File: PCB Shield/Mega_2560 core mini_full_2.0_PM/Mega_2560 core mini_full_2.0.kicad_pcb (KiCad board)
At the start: 2 copper layers, 89.5 x 59.7 mm, 110 parts, among them P1 2560-core, P10 SPI_libre, P11 Trim, P12 Stick_left, P13 Stick_right, P14 Switch, P15 LCD_I2C, P16 LCD, P17 Battery LIPO, P18 Ecolage, P19 Module_TX, P2 Clock, P20 Module_RS232/TTL, P21 Sw_power, P22 CONN_JQ6500_28P_mini, P23 Rot_1, P24 Rot_2, P25 Key_select_menu_ESC, P26 LCD_Vcc_select, P27 HP, P28 5v/3,3v manches, P3 Option, P4 Potentiometre, P5 Vibreur, P6 Micro_sd, P7 Option, P8 Audio, P9 SPI, U1 4066, U2 TLP290, U3 TLP290, U4 L4941, U5 LD1117S33TR, U6 MCP604-I/SL

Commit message: Update _Mega_2560 core mini_full_2.0_PM
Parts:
- removed the P8 at (205.6, 64.4)
- added C12: 100nF, Capacitors_SMD:C_1206, B.Cu at (150.6, 111.5)
- added C13: 100nF, Capacitors_SMD:C_1206, B.Cu at (149.8, 101.1)
- added C14: 100nF, Capacitors_SMD:C_1206, F.Cu at (149.8, 101.1)
- added P24: Rot_2, Pin_Headers:Pin_Header_Straight_1x04_Pitch2.54mm, F.Cu at (226.5, 112.7)
- added P29: RXTX, Pin_Headers:Pin_Header_Straight_1x04_Pitch2.54mm, F.Cu at (210.7, 98.7)
- added P30: MiniDCDC3A, MegaCore_Shield:MiniDCDC3A, F.Cu at (208.8, 64.4)
- C10, C11, C5, C9, P21: moved to B.Cu
- P12, P13: footprint Pin_Headers:Pin_Header_Straight_1x04_Pitch2.54mm -> MegaCore_Shield:Pin_Header_Straight_2x03_Pitch2.54mm
- P17: value Battery LIPO -> BATT
- P20: value Module_RS232/TTL -> TTL/RS232; footprint anthoperso:Con_RS232_TTL -> MegaCore_Shield:Con_RS232_TTL
- P25: value Key_select_menu_ESC -> Keys
- P26: value LCD_Vcc_select -> LCD_Alim
- P4: value Potentiometre -> 3 Pots; footprint Pin_Headers:Pin_Header_Straight_2x05_Pitch2.54mm -> MegaCore_Shield:Pin_Header_Straight_3x03_Pitch2.54mm
- P7: value Option -> HF_modules; footprint Pin_Headers:Pin_Header_Straight_1x06_Pitch2.54mm -> MegaCore_Shield:Pin_Header_Straight_1x09_Pitch2.54mm
- P8: renamed from P24; value Rot_2 -> Audio
- R7: moved to F.Cu
- U2: footprint anthoperso:SOP4 -> MegaCore_Shield:SOP4
- moved P8 52.6 mm to (205.6, 64.4), turned to 0 degrees
- moved R9 19.1 mm to (194.8, 111.4)
- moved P17 15.9 mm to (205.6, 78.4), turned to 180 degrees
- moved C2 15.5 mm to (218.5, 103.8)
- moved P26 14.6 mm to (226.5, 101.9), turned to 270 degrees
- moved RV6 14.4 mm to (159.9, 66.3), turned to 180 degrees
- moved P3 12.8 mm to (216.4, 110.1)
- moved D2 11.7 mm to (218.3, 91.1)
- moved P19 5.68 mm to (218.3, 88.5)
- moved R7 5.43 mm to (218.3, 93.6)
- moved RV1 4.62 mm to (149.7, 115.2), turned to 180 degrees
- moved C9 4.58 mm to (144.0, 70.8)
- moved C11 4.37 mm to (144.0, 80.7)
- moved C17 3.70 mm to (148.4, 80.3), turned to 270 degrees
- moved P25 3.59 mm to (205.6, 88.5), turned to 90 degrees
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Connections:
- net Net-(C28-Pad1) renamed /DCDC_IN+
- net Net-(P17-Pad2) renamed /LIPO+
- C11 pad 1: /Power_manches -> /Stick_LHcon
- C11 pad 2: /Stick_LVcon -> GND
- C16 pad 1: /Power_manches -> /Stick_RHcon
- C16 pad 2: /Stick_RHcon -> GND
- C17 pad 1: /Power_manches -> /Stick_RVcon
- C17 pad 2: /Stick_RVcon -> GND
- C9 pad 1: /Power_manches -> /Stick_LVcon
- C9 pad 2: /Stick_LHcon -> GND
- D6 pad 2: +BATT -> /R16_R17
- P1 pad D4: (no net) -> /CS_CYRF6936
- P12 pad 2: /Stick_LHcon -> /Power_manches
- P12 pad 4: GND -> /Stick_LHcon
- P13 pad 2: /Stick_RHcon -> /Power_manches
- P13 pad 3: /Stick_RVcon -> /Stick_RHcon
- P13 pad 4: GND -> /Stick_RVcon
- P20 pad 1: GND -> /RX_module
- P20 pad 2: VCC -> /TX_module
- P20 pad 3: Net-(P20-Pad3) -> VCC
- P20 pad 4: Net-(P20-Pad4) -> GND
- P20 pad 5: GND -> Net-(P20-Pad5)
- P20 pad 6: VCC -> Net-(P20-Pad6)
- P20 pad 7: /TX_module -> VCC
- P20 pad 8: /RX_module -> GND
- P21 pad 1: +BATT -> /R16_R17
- P4 pad 2: /Pot_2 -> /Pot_3
- P4 pad 3: VCC -> GND
- P4 pad 4: /Pot_3 -> VCC
- P4 pad 5: VCC -> /Pot_2
- P4 pad 6: /Pot_1 -> GND
- P4 pad 7: GND -> VCC
- P4 pad 8: GND -> /Pot_1
- P7 pad 1: /Microsd_CS -> /P3_3V
- P7 pad 2: /Sck -> GND
- P7 pad 3: /Mosi -> /Sck
- P7 pad 4: /Miso -> /Mosi
- P7 pad 5: VCC -> /Miso
- P7 pad 6: GND -> /CS_CYRF6936
- P8 pad 1: /Rot_2push -> Net-(P8-Pad1)
- P8 pad 2: /Rot_2B -> Net-(P8-Pad2)
- P8 pad 3: /Rot_2A -> VCC
- R17 pad 2: +BATT -> /R16_R17
- U2 pad 3: Net-(P20-Pad3) -> Net-(P20-Pad6)
- U3 pad 4: Net-(P20-Pad4) -> Net-(P20-Pad5)
- U5 pad 4: (no net) -> /P3_3V
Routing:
- net +BATT: track 35.7 -> 6.53 mm
- net /P3_3V: track 105.3 -> 129.4 mm, vias 4 -> 2
- net GND: track 77.9 -> 101.3 mm, vias 20 -> 16
- net /Vibreur: track 2.36 -> 22.3 mm
- net Net-(D1-Pad1): track 32.4 -> 13.4 mm
- net /Lcd_bla: track 42.7 -> 26.2 mm, vias 2 -> 0
- net Net-(P16-Pad18): track 34.7 -> 48.9 mm, vias 3 -> 4
- net /PPM_out: track 39.3 -> 53.3 mm
- net /R16_R17: track 0.00 -> 11.7 mm
- net /Key_ESC: track 6.77 -> 18.4 mm, vias 0 -> 1
- net VCC: track 376.4 -> 387.4 mm, vias 12 -> 14
- net /Key_MENU: track 6.77 -> 17.7 mm, vias 0 -> 1
- net /Lcd_A0: track 69.7 -> 59.4 mm
- net /DCDC_IN+: track 12.1 -> 22.3 mm
- net Net-(P20-Pad6): track 0.00 -> 9.97 mm
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- added copper zone on B.Cu, net /P3_3V
- added copper zone on F.Cu, net /P3_3V
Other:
- board text added: "5 3,3"
- board text added: "By OpenAVRc Team"
- board text added: "ICSP"
- board text added: "MegaCore2560 Shield V2.0"
- board text removed: "3.3v"
- board text removed: "MegaCore2560 Shield"
- board text removed: "OpenAVRc Team V2.0"

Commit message: Update_Mega_2560 core mini_full_2.0_PM_23-8-2017
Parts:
- added BT1: CR2032, Pin_Headers:Pin_Header_Straight_1x02_Pitch2.54mm, F.Cu at (197.3, 106.3)
- added C15: 100nF, Capacitors_SMD:C_1206, F.Cu at (197.5, 116.1)
- added C18: 100nF, Capacitors_SMD:C_1206, F.Cu at (175.0, 82.1)
- added C19: 100nF, Capacitors_SMD:C_1206, B.Cu at (167.1, 117.3)
- added C20: 100nF, Capacitors_SMD:C_1206, B.Cu at (178.5, 117.5)
- added C21: 100nF, Capacitors_SMD:C_1206, B.Cu at (193.3, 117.5)
- added C22: 100nF, Capacitors_SMD:C_1206, B.Cu at (184.6, 99.3)
- added C23: 100nF, Capacitors_SMD:C_1206, B.Cu at (181.5, 106.3)
- added D3: LL4148, MegaCore_Shield:D_SCD80_HandSoldering, F.Cu at (192.9, 94.9)
- added D4: LL4148, MegaCore_Shield:D_SCD80_HandSoldering, F.Cu at (192.9, 96.4)
- added P31: Pot2, Pin_Headers:Pin_Header_Straight_1x03_Pitch2.54mm, F.Cu at (154.1, 106.3)
- added P32: Pot1, Pin_Headers:Pin_Header_Straight_1x03_Pitch2.54mm, F.Cu at (154.1, 103.8)
- added R10: 22K, Resistors_SMD:R_1206, B.Cu at (200.5, 67.0)
- added R15: 10K, anthoperso:R_1206, B.Cu at (186.5, 107.0)
- added R20: 10K, anthoperso:R_1206, B.Cu at (186.5, 103.2)
- added REF**: SOIC-Micro8, MegaCore_Shield:SOIC-Micro8, F.Cu at (243.0, 69.5)
- added REF**: SOT-457, MegaCore_Shield:SOT-457, F.Cu at (243.0, 77.1)
- added U7: FM24W256, MegaCore_Shield:SOIC-8-FRAM_DI, F.Cu at (185.9, 100.0)
- added U8: DS3231, MegaCore_Shield:SO-16-DS3231, F.Cu at (185.9, 108.2)
- added U9: 4050, MegaCore_Shield:SO-16-N, F.Cu at (243.0, 87.9)
- P4: value 3 Pots -> Pot3; footprint MegaCore_Shield:Pin_Header_Straight_3x03_Pitch2.54mm -> Pin_Headers:Pin_Header_Straight_1x03_Pitch2.54mm
- P7: value HF_modules -> SPIX; footprint MegaCore_Shield:Pin_Header_Straight_1x09_Pitch2.54mm -> MegaCore_Shield:Pin_Header_Straight_2x05_Pitch2.54mm
- R2: value 22K -> 1K
- U1: value 4066 -> 74LVC1G3157; footprint Librairie master:SOP14 -> MegaCore_Shield:SOT-363_SC-70-6_Handsoldering
- moved R5 60.0 mm to (238.5, 99.1)
- moved R6 59.8 mm to (244.3, 99.1), turned to 90 degrees
- moved C6 32.7 mm to (192.2, 77.8)
- moved R16 15.9 mm to (208.8, 78.4), turned to 270 degrees
- moved R3 15.4 mm to (176.4, 101.2), turned to 180 degrees
- moved R17 15.3 mm to (211.3, 78.4), turned to 90 degrees
- moved U1 9.09 mm to (184.0, 116.5), turned to 0 degrees
- moved R4 4.49 mm to (178.9, 92.4)
- moved P27 4.07 mm to (197.3, 78.4), turned to 180 degrees
- moved R9 2.90 mm to (197.3, 110.0), turned to 90 degrees
- moved C12 2.85 mm to (149.1, 113.9)
- moved P7 2.84 mm to (179.5, 76.5)
- moved RV1 2.54 mm to (149.7, 117.8)
- moved C38 1.91 mm to (215.1, 75.2)
- moved R8 1.71 mm to (193.5, 110.0), turned to 270 degrees
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- renumbered REF** to Fix1, REF** to Fix2, REF** to Fix3
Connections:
- C38 pad 1: /P3_3V -> P3_3V
- C8 pad 1: /P3_3V -> P3_3V
- D2 pad 2: /PPM_out -> /Master_PPMout
- D6 pad 2: /R16_R17 -> +BATT
- P1 pad A0: /Trim_RH-> -> /Lcd_db0
- P1 pad A1: /Trim_RH<- -> /Lcd_db1
- P1 pad A2: /Trim_RV-> -> /Lcd_db2
- P1 pad A3: /Trim_RV<- -> /Lcd_db3
- P1 pad A4: /Trim_LV-> -> /Lcd_db4
- P1 pad A5: /Trim_LV<- -> /Lcd_db5
- P1 pad A6: /Trim_LH-> -> /Lcd_db6
- P1 pad A7: /Trim_LH<- -> /Lcd_db7
- P1 pad D4: /CS_CYRF6936 -> /PPM_in
- P10 pad 1: /PH2 -> (no net)
- P10 pad 2: /TXD2 -> (no net)
- P10 pad 3: /RXD2 -> (no net)
- P15 pad 3: /Sda -> /SDA
- P15 pad 4: /Scl -> /SCL
- P2 pad 1: /Scl -> /SCL
- P2 pad 2: /Sda -> /SDA
- P21 pad 1: /R16_R17 -> +BATT
- P26 pad 1: /P3_3V -> P3_3V
- P28 pad 3: /P3_3V -> P3_3V
- P3 pad 1: /Scl -> /SCL
- P3 pad 2: /Sda -> /SDA
- P7 pad 1: /P3_3V -> /CS_CC2500
- P7 pad 2: GND -> /CS_CYRF6936
- P7 pad 3: /Sck -> /CS_A7105
- P7 pad 4: /Mosi -> /CS_NRF24L01
- P7 pad 5: /Miso -> /Xmitter_MISO
- P7 pad 6: /CS_CYRF6936 -> /Xmitter_SCK
- P7 pad 7: (no net) -> P3_3V
- P7 pad 8: (no net) -> /Xmitter_MOSI
- P7 pad 9: (no net) -> GND
- R17 pad 2: /R16_R17 -> +BATT
- R3 pad 1: /core_pw10 -> /JQ6500Busy
- R4 pad 1: /core_pw13 -> /JQ6500Data
- R5 pad 1: VCC -> (no net)
- R5 pad 2: Net-(R5-Pad2) -> (no net)
- R6 pad 1: GND -> (no net)
- R6 pad 2: Net-(R6-Pad2) -> (no net)
- U1 pad 1: GND -> /PPM_in
- U1 pad 2: Net-(R5-Pad2) -> GND
- U1 pad 3: Net-(R6-Pad2) -> /Master_PPMout
- U1 pad 4: VCC -> Net-(R8-Pad2)
- U1 pad 5: /Sim_control -> VCC
- U1 pad 6: Net-(R5-Pad2) -> /Sim_Control
- U5 pad 2: /P3_3V -> P3_3V
- U5 pad 4: /P3_3V -> P3_3V
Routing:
- net P3_3V: track 0.00 -> 133.1 mm, vias 0 -> 3
- net /P3_3V: track 129.4 -> 0.00 mm, vias 2 -> 0
- net /Master_PPMout: track 0.00 -> 69.4 mm, vias 0 -> 4
- net GND: track 101.3 -> 160.0 mm, vias 16 -> 21
- net /PPM_out: track 53.3 -> 0.00 mm, vias 2 -> 0
- net /Sim_Control: track 0.00 -> 47.9 mm, vias 0 -> 4
- net /SDA: track 0.00 -> 43.6 mm, vias 0 -> 3
- net /SCL: track 0.00 -> 41.0 mm, vias 0 -> 2
- net /Xmitter_MISO: track 0.00 -> 40.7 mm, vias 0 -> 2
- net /Sim_control: track 36.8 -> 0.00 mm, vias 4 -> 0
- net /JQ6500Data: track 0.00 -> 34.3 mm, vias 0 -> 1
- net /Xmitter_MOSI: track 0.00 -> 34.0 mm, vias 0 -> 2
- net /Xmitter_SCK: track 0.00 -> 29.9 mm, vias 0 -> 3
- net /CS_A7105: track 0.00 -> 29.8 mm, vias 0 -> 2
- net /CS_NRF24L01: track 0.00 -> 29.3 mm, vias 0 -> 2
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- added copper zone on B.Cu, net P3_3V
- added copper zone on F.Cu, net P3_3V
- removed copper zone on B.Cu, net /P3_3V
- removed copper zone on F.Cu, net /P3_3V
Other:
- board text added: "+"
- board text added: "-"

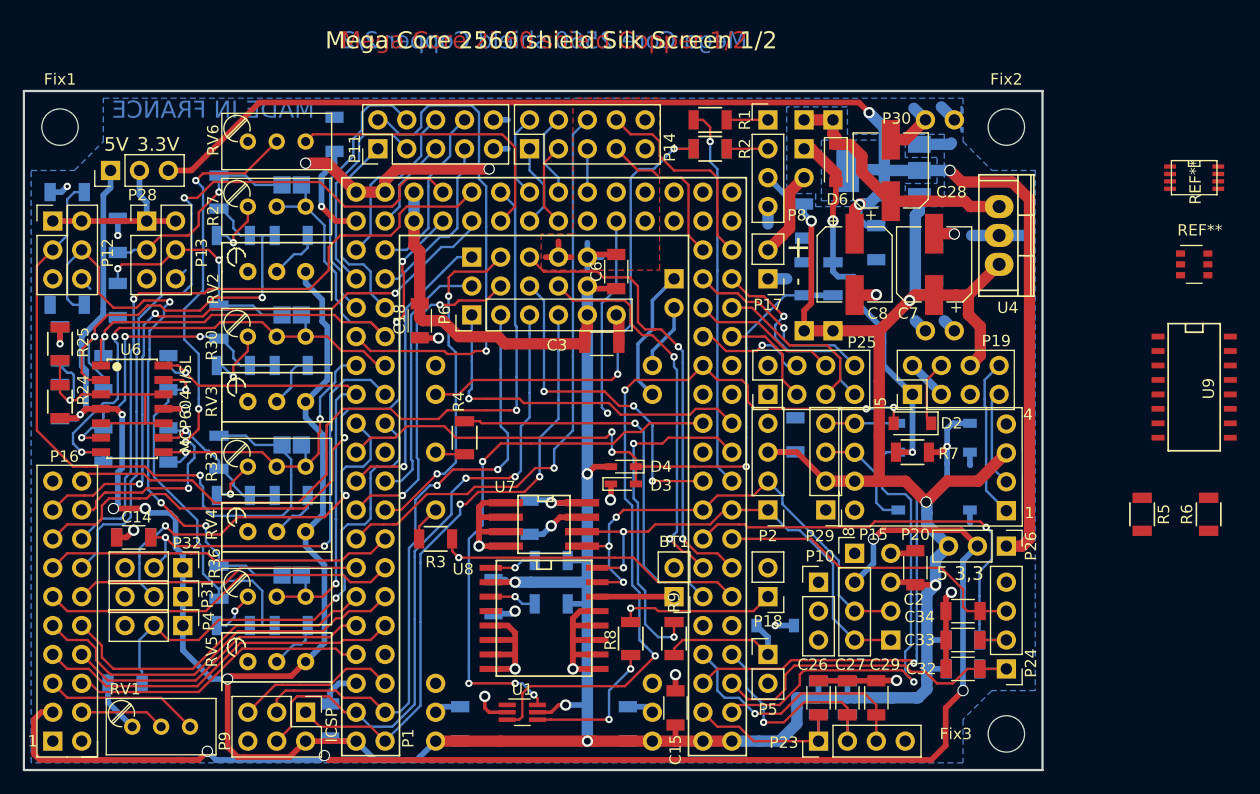
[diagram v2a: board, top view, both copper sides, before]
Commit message: Update schematic R values
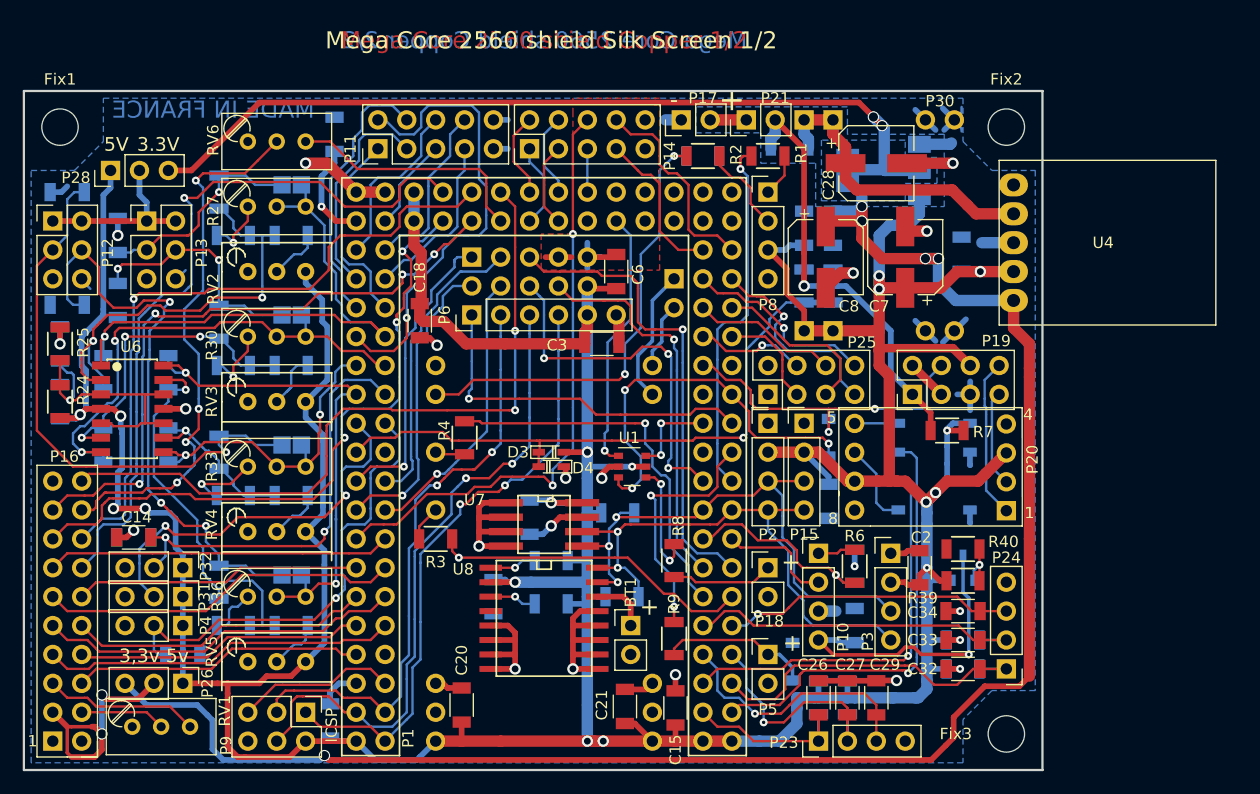
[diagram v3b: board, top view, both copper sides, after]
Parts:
- removed the P10 at (210.0, 105.1)
- removed REF**: SOIC-Micro8, MegaCore_Shield:SOIC-Micro8
- removed the U1 at (184.0, 116.5)
- removed U9: 4050, MegaCore_Shield:SO-16-N
- added C24: 100nF, Capacitors_SMD:C_1206, B.Cu at (213.2, 108.9)
- added Q1: BSS84, MegaCore_Shield:SOT-23_MOS_P, B.Cu at (222.7, 103.8)
- added R21: 4,7K, anthoperso:R_1206, B.Cu at (192.4, 99.0)
- added R38: 4,7K, anthoperso:R_1206, B.Cu at (192.8, 106.3)
- added R39: 47K, Resistors_SMD:R_1206, F.Cu at (222.7, 104.9)
- added R40: 100, Resistors_SMD:R_1206, F.Cu at (222.7, 102.1)
- C1, C2, C3, C5: value 47nF -> 100nF
- C20, C21, P21, P3: moved to F.Cu
- C28, C7: value 47µF -> 100µF
- D2, D6: moved to B.Cu
- P10: renamed from P29; value RXTX -> RX1TX1
- P22: value CONN_JQ6500_28P_mini -> JQ6500_28P
- R11, R12, R13, R14: value 15K -> 120K
- R18, R19, R22, R23: value 5.1k -> 5.1K
- R24: value 33K -> 82K
- R25: value 33K -> 39K
- R26, R29, R32, R35: value 10K -> 47K
- R27, R30, R33, R36: value POT_22k -> 100K
- R28, R31, R34, R37: value 10K -> 120K
- R5: value 10K -> 4K7; moved to B.Cu
- R6: value 10K -> 4K7
- RV2, RV3, RV4, RV5: value POT_100k -> 100K
- U1: renamed from REF**; value SOT-457 -> 74LVC1G3157GV
- U4: value L4941 -> PM5033; footprint Power_Integrations:TO-220 -> MegaCore_Shield:Pm5033_sil5
- U8: value DS3231 -> DS3231SN
- moved P26 73.4 mm to (154.1, 113.9)
- moved U1 52.5 mm to (193.6, 94.9)
- moved R6 31.4 mm to (213.2, 103.7)
- moved R5 25.7 mm to (213.2, 103.7)
- moved P17 15.9 mm to (198.0, 64.4), turned to 90 degrees
- moved P15 12.3 mm to (208.8, 91.1)
- moved R8 7.85 mm to (197.3, 103.2), turned to 90 degrees
- moved P2 7.62 mm to (205.6, 91.1), turned to 0 degrees
- moved P3 7.62 mm to (216.4, 102.5)
- moved D2 7.47 mm to (210.9, 92.4), turned to 270 degrees
- moved C1 6.53 mm to (210.9, 97.9), turned to 90 degrees
- moved D4 6.53 mm to (186.5, 94.9), turned to 180 degrees
- moved D3 6.48 mm to (186.5, 93.6), turned to 0 degrees
- moved P8 6.35 mm to (205.6, 70.8)
- moved R1 5.99 mm to (205.6, 67.6)
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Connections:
- net /CS_CC2500 renamed CS_CC2500
- net /Isp_rst renamed /OpenAVRc_CoreConnects/Isp_rst
- net /JQ6500Busy renamed JQ6500Busy
- net /JQ6500Data renamed JQ6500Data
- net /Key_DOWN renamed Key_DOWN
- net /Key_ESC renamed Key_ESC
- net /Key_LEFT renamed Key_LEFT
- net /Key_MENU renamed Key_MENU
- net /Key_RIGHT renamed Key_RIGHT
- net /Key_UP renamed Key_UP
- net /Lcd_A0 renamed /OpenAVRc_CoreConnects/Lcd_A0
- net /Lcd_bla renamed /OpenAVRc_CoreConnects/Lcd_bla
- net /Lcd_cs renamed /OpenAVRc_CoreConnects/Lcd_cs
- net /Lcd_db0 renamed /OpenAVRc_CoreConnects/Lcd_db0
- net /Lcd_db1 renamed /OpenAVRc_CoreConnects/Lcd_db1
- net /Lcd_db2 renamed /OpenAVRc_CoreConnects/Lcd_db2
- net /Lcd_db3 renamed /OpenAVRc_CoreConnects/Lcd_db3
- net /Lcd_db4 renamed /OpenAVRc_CoreConnects/Lcd_db4
- net /Lcd_db5 renamed /OpenAVRc_CoreConnects/Lcd_db5
- net /Lcd_db6 renamed /OpenAVRc_CoreConnects/Lcd_db6
- net /Lcd_db7 renamed /OpenAVRc_CoreConnects/Lcd_db7
- net /Lcd_e renamed /OpenAVRc_CoreConnects/Lcd_e
- net /Lcd_r/w renamed /OpenAVRc_CoreConnects/Lcd_r/w
- net /Lcd_rst renamed /OpenAVRc_CoreConnects/Lcd_rst
- net /Lcd_vo renamed /OpenAVRc_CoreConnects/Lcd_vo
- net /Microsd_CS renamed /OpenAVRc_CoreConnects/Microsd_CS
- net /Miso renamed /OpenAVRc_CoreConnects/Miso
- net /Mosi renamed /OpenAVRc_CoreConnects/Mosi
- net /Pot_1 renamed Pot_1
- net /Pot_2 renamed Pot_2
- net /Pot_3 renamed Pot_3
- net /Power_manches renamed /OpenAVRc_Sticks/Power_manches
- net /RX_module renamed /OpenAVRc_HF_Telemetry/RX_module
- net /Rot_1A renamed Rot_1A
- net /Rot_1B renamed Rot_1B
- net /Rot_1push renamed Rot_1push
- net /Rot_2push renamed Rot_2push
- net /Sck renamed /OpenAVRc_CoreConnects/Sck
- net /Stick_LH renamed Stick_LH
- net /Stick_LHcon renamed /OpenAVRc_Sticks/Stick_LHcon
- net /Stick_LV renamed Stick_LV
- net /Stick_LVcon renamed /OpenAVRc_Sticks/Stick_LVcon
- net /Stick_RH renamed Stick_RH
- net /Stick_RHcon renamed /OpenAVRc_Sticks/Stick_RHcon
- net /Stick_RV renamed Stick_RV
- net /Stick_RVcon renamed /OpenAVRc_Sticks/Stick_RVcon
- net /Sw_ailDR renamed Sw_ailDR
- net /Sw_eleDR renamed Sw_eleDR
- net /Sw_gear renamed Sw_gear
- net /Sw_id1 renamed Sw_id1
- net /Sw_id2 renamed Sw_id2
- net /Sw_rudDR renamed Sw_rudDR
- net /Sw_thcut renamed Sw_thcut
- net /Sw_turn renamed Sw_turn
- net /TX_module renamed /OpenAVRc_HF_Telemetry/TX_module
- net /Tele_RX renamed Tele_RX
- net /Tele_TX renamed Tele_TX
- net /Trim_LH-> renamed Trim_LH->
- net /Trim_LH<- renamed Trim_LH<-
- net /Trim_LV-> renamed Trim_LV->
- net /Trim_LV<- renamed Trim_LV<-
- net /Trim_RH-> renamed Trim_RH->
- net /Trim_RH<- renamed Trim_RH<-
- net /Trim_RV-> renamed Trim_RV->
- net /Trim_RV<- renamed Trim_RV<-
- net /VREF renamed /OpenAVRc_CoreConnects/VREF
- net /Vibreur renamed Vibreur
- net /Xmitter_MISO renamed Xmitter_MISO
- net /Xmitter_MOSI renamed Xmitter_MOSI
- net /Xmitter_SCK renamed Xmitter_SCK
- net /audio_left_in renamed Audio_Buzzer_out
- net /audio_right_in renamed /OpenAVRc_Audio_Haptic/JQ_Left_Out
- C28 pad 1: /DCDC_IN+ -> /OpenAVRc_Power/DCDC_IN+
- C33 pad 1: /Rot_2B -> Rot_2B
- C34 pad 1: /Rot_2A -> Rot_2A
- C38 pad 1: P3_3V -> +3.3V
- C8 pad 1: P3_3V -> +3.3V
- D2 pad 1: /PPM_TX_OUT -> Master_PPMout
- D2 pad 2: /Master_PPMout -> PPM16_SIMout
- D3 pad 1: /U_batt -> U_batt
- D4 pad 2: /U_batt -> U_batt
- D6 pad 1: /DCDC_IN+ -> /OpenAVRc_Power/DCDC_IN+
- P1 pad AC15: /U_batt -> U_batt
- P1 pad B5: (no net) -> PPM16_SIMout
- P1 pad B6: /Master_PPMout -> Master_PPMout
- P1 pad D0: /SCL -> Scl
- P1 pad D1: /SDA -> Sda
- P1 pad D2: /Rot_2A -> BT_Rxd1
- P1 pad D3: /Rot_2B -> BT_Txd1
- P1 pad D4: /PPM_in -> PPM_in
- P1 pad E6: (no net) -> Rot_2B
- P1 pad E7: (no net) -> Rot_2A
- P1 pad H6: /Sim_Control -> Sim_Control
- P1 pad J4: /CS_CYRF6936 -> CS_CYRF6936
- P1 pad J5: /CS_NRF24L01 -> CS_NRF24L01
- P1 pad J6: /CS_A7105 -> CS_A7105
- P10 pad 1: GND -> Net-(P10-Pad1)
- P10 pad 2: VCC -> BT_Rxd1
- P10 pad 3: Net-(P20-Pad6) -> GND
- P10 pad 4: Net-(P20-Pad5) -> Net-(C24-Pad1)
- P15 pad 2: /LCD_VCC -> VCC
- P15 pad 3: /SDA -> Sda
- P15 pad 4: /SCL -> Scl
- P16 pad 3: /LCD_VCC -> LCD_VCC
- P17 pad 2: /LIPO+ -> /OpenAVRc_Power/LIPO+
- P19 pad 4: /PPM_TX_OUT -> Master_PPMout
- P2 pad 1: /SCL -> GND
- P2 pad 2: /SDA -> VCC
- P2 pad 3: VCC -> Sda
- P2 pad 4: GND -> Scl
- P21 pad 1: +BATT -> /OpenAVRc_Power/LIPO+
- P21 pad 2: /LIPO+ -> +BATT
- P24 pad 2: /Rot_2B -> Rot_2B
- P24 pad 3: /Rot_2A -> Rot_2A
- P26 pad 1: P3_3V -> VCC
- P26 pad 2: /LCD_VCC -> LCD_VCC
- P26 pad 3: VCC -> +3.3V
- P28 pad 3: P3_3V -> +3.3V
- P3 pad 1: /SCL -> GND
- P3 pad 2: /SDA -> VCC
- P3 pad 3: VCC -> Sda
- P3 pad 4: GND -> Scl
- P30 pad 3: /DCDC_IN+ -> /OpenAVRc_Power/DCDC_IN+
- P30 pad 4: /DCDC_IN+ -> /OpenAVRc_Power/DCDC_IN+
- P7 pad 2: /CS_CYRF6936 -> CS_NRF24L01
- P7 pad 3: /CS_A7105 -> CS_CYRF6936
- P7 pad 4: /CS_NRF24L01 -> CS_A7105
- P7 pad 7: P3_3V -> +3.3V
- R16 pad 1: GND -> U_batt
- R16 pad 2: /U_batt -> GND
- R17 pad 1: /U_batt -> U_batt
- R22 pad 2: /Rot_2B -> Rot_2B
- R5 pad 1: (no net) -> BT_Txd1
- R5 pad 2: (no net) -> GND
- R6 pad 1: (no net) -> BT_Txd1
- R6 pad 2: (no net) -> Net-(P10-Pad1)
- U1 pad 1: (no net) -> PPM_in
- U1 pad 2: (no net) -> GND
- U1 pad 3: (no net) -> PPM16_SIMout
- U1 pad 4: (no net) -> Net-(R8-Pad2)
- U1 pad 5: (no net) -> VCC
- U1 pad 6: (no net) -> Sim_Control
- U4 pad 1: /DCDC_IN+ -> (no net)
- U4 pad 2: GND -> /OpenAVRc_Power/DCDC_IN+
- U4 pad 3: VCC -> GND
- U5 pad 2: P3_3V -> +3.3V
- U5 pad 4: P3_3V -> +3.3V
- U7 pad 5: /SDA -> Sda
- U7 pad 6: /SCL -> Scl
- U8 pad 15: /SDA -> Sda
- U8 pad 16: /SCL -> Scl
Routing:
- net +3.3V: track 0.00 -> 231.1 mm, vias 0 -> 7
- net P3_3V: track 133.1 -> 0.00 mm, vias 3 -> 0
- net /LCD_VCC: track 120.0 -> 0.00 mm, vias 4 -> 0
- net /Master_PPMout: track 69.4 -> 0.00 mm, vias 4 -> 0
- net /U_batt: track 60.8 -> 0.00 mm, vias 3 -> 0
- net U_batt: track 0.00 -> 55.1 mm, vias 0 -> 1
- net Sda: track 0.00 -> 49.4 mm, vias 0 -> 3
- net Scl: track 0.00 -> 48.1 mm, vias 0 -> 2
- net /Sim_Control: track 47.9 -> 0.00 mm, vias 4 -> 0
- net /SDA: track 43.6 -> 0.00 mm, vias 3 -> 0
- net Net-(C24-Pad1): track 0.00 -> 42.2 mm, vias 0 -> 1
- net /Rot_2B: track 41.2 -> 0.00 mm, vias 1 -> 0
- net /SCL: track 41.0 -> 0.00 mm, vias 2 -> 0
- net PPM16_SIMout: track 0.00 -> 34.2 mm, vias 0 -> 3
- net Rot_2B: track 0.00 -> 30.6 mm
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- added copper zone on B.Cu, net +3.3V
- added copper zone on F.Cu, net +3.3V
- removed copper zone on B.Cu, net P3_3V
- removed copper zone on F.Cu, net P3_3V
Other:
- net class Alimentation: via_dia 1 -> 0.7; via_drill 0.6 -> 0.3
- net class Default: via_dia 0.65 -> 0.7
- net class LCDVCC: via_dia 0.65 -> 0.7
- rule via_min_size: 0.65 -> 0.7
- board text added: "3,3v 5v"
- board text removed: "5 3,3"
